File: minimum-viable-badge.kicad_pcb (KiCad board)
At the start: 2 copper layers, 100 x 64 mm, 34 parts, among them P1 BATTERY, P11 MECH, P12 MECH, P13 MECH, P2 USB, P301 eInk, Q1 S8050, Q2 S8050, SW3 ON|OFF, U1 CP2102, U2 ESP32-WROOM, U3 NCP5501, U4 MCP73831

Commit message: PCB new outline added
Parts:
- SW3: value ON|OFF -> OFF|ON
- moved P13 157.1 mm to (26.2, 93.9)
- moved P11 156.8 mm to (26.5, 41.8)
- moved P301 153.1 mm to (45.0, 60.5)
- moved U2 139.7 mm to (124.6, 84.5), turned to 45 degrees
- moved P12 137.2 mm to (133.5, 42.5)
- moved P2 73.9 mm to (124.2, 38.5), turned to 270 degrees
- moved SW3 73.3 mm to (110.6, 40.1), turned to 0 degrees
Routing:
- net (no net): track 203.8 -> 0.00 mm
- net /USB_VCC: track 182.7 -> 0.00 mm, vias 4 -> 0
- net +3V3: track 166.8 -> 0.00 mm, vias 2 -> 0
- net /BAT+: track 91.3 -> 0.00 mm, vias 2 -> 0
- net /USB_D+: track 90.1 -> 0.00 mm, vias 1 -> 0
- net /USB_D-: track 90.0 -> 0.00 mm, vias 1 -> 0
- net GND: track 75.8 -> 0.00 mm, vias 12 -> 0
- net /IO32: track 74.1 -> 0.00 mm
- net /IO33: track 72.5 -> 0.00 mm
- net /IO15: track 70.8 -> 0.00 mm, vias 1 -> 0
- net /D/C: track 70.7 -> 0.00 mm
- net /DTR: track 69.6 -> 0.00 mm, vias 2 -> 0
- net /IO12: track 69.6 -> 0.00 mm, vias 1 -> 0
- net /IO26: track 68.9 -> 0.00 mm
- net /CS: track 67.4 -> 0.00 mm
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- removed copper zone on B.Cu, net GND
- removed copper zone on F.Cu, net GND
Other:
- board size 100 x 64 mm -> 256.9 x 71.3 mm

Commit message: Placement started
Predicting Bob will end up changing all this
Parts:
- removed C1, C3: 10uF, Capacitors_SMD:C_0805_HandSoldering
- removed C13, C16: 4u7, Capacitors_SMD:C_0805_HandSoldering
- removed C14, C2, C4: 0.1uF, Capacitors_SMD:C_0603_HandSoldering
- removed C15: 100uF, Capacitors_SMD:C_1210_HandSoldering
- removed D1, D2: SS14, Diodes_SMD:D_SMA
- removed D3: CHRG, LEDs:LED_0603
- removed F1: 1A PTC, Diodes_SMD:D_1206
- removed P1: BATTERY, Pin_Headers:Pin_Header_Angled_1x02_Pitch2.54mm
- removed P11, P12, P13: MECH, Mounting_Holes:MountingHole_3.2mm_M3_Pad
- removed P2: USB, libs:USB-MICRO-5pin_PTHMOUNT-Amphenol.10118194-0001LF
- removed Q1, Q2: S8050, TO_SOT_Packages_SMD:SOT-23_Handsoldering
- removed R1: 1M, Resistors_SMD:R_0603_HandSoldering
- removed R10, R6: 470R, Resistors_SMD:R_0603_HandSoldering
- removed R12: 2K, Resistors_SMD:R_0603_HandSoldering
- removed R2: 100K, Resistors_SMD:R_0603_HandSoldering
- removed R3, R4: 12K(1%), Resistors_SMD:R_0603_HandSoldering
- removed R5: 10K, Resistors_SMD:R_0603_HandSoldering
- removed R7: 12K, Resistors_SMD:R_0603_HandSoldering
- removed SW3: OFF|ON, libs:SS12D00
- removed U1: CP2102, Housings_DFN_QFN:QFN-28-1EP_5x5mm_Pitch0.5mm
- removed U2: ESP32-WROOM, ESP32-footprints-Lib:ESP32-WROOM
- removed U3: NCP5501, libs:DPAK3.NCP5501
- removed U4: MCP73831, TO_SOT_Packages_SMD:SOT-23-5_HandSoldering
- added C101: 1uF, Capacitors_SMD:C_0603_HandSoldering, F.Cu at (129.9, 134.2)
- added C102: 1uF, Capacitors_SMD:C_0603_HandSoldering, F.Cu at (137.3, 133.5)
- added C103: 1uF, Capacitors_SMD:C_0603_HandSoldering, F.Cu at (135.8, 75.3)
- added C104: 10uF, Capacitors_SMD:C_0805_HandSoldering, F.Cu at (129.6, 60.8)
- added C105: 0.1uF, Capacitors_SMD:C_0603_HandSoldering, F.Cu at (129.7, 56.2)
- added C106: 10uF, Capacitors_SMD:C_0805_HandSoldering, F.Cu at (135.7, 65.2)
- added C107: 0.1uF, Capacitors_SMD:C_0603_HandSoldering, F.Cu at (135.9, 60.2)
- added C201: 4u7, Capacitors_SMD:C_0805_HandSoldering, F.Cu at (112.8, 43.6)
- added C202: 4u7, Capacitors_SMD:C_0805_HandSoldering, F.Cu at (99.7, 45.2)
- added C203: 0.1uF, Capacitors_SMD:C_0603_HandSoldering, F.Cu at (56.2, 45.8)
- added C204: 100uF, Capacitors_SMD:C_1210_HandSoldering, F.Cu at (55.9, 40.0)
- added C301: 1uF, Capacitors_SMD:C_0603_HandSoldering, F.Cu at (73.8, 182.4)
- added C302: 1uF 50V, Capacitors_SMD:C_0603_HandSoldering, F.Cu at (77.2, 167.8)
- added C303: 1uF 50V, Capacitors_SMD:C_0603_HandSoldering, F.Cu at (64.1, 182.1)
- added C304: 1uF, Capacitors_SMD:C_0603_HandSoldering, F.Cu at (67.2, 186.9)
- added C305: 1uF, Capacitors_SMD:C_0603_HandSoldering, F.Cu at (80.7, 172.6)
- added C306: 4.7uF 50V, Capacitors_SMD:C_0603_HandSoldering, F.Cu at (49.1, 186.3)
- added C307: 10uF 6.3V, Capacitors_SMD:C_0805_HandSoldering, F.Cu at (57.4, 175.3)
- added C308: 1uF, Capacitors_SMD:C_0603_HandSoldering, F.Cu at (75.3, 177.6)
- added C309: 1uF, Capacitors_SMD:C_0603_HandSoldering, F.Cu at (69.5, 182.1)
- added C310: 1uF, Capacitors_SMD:C_0603_HandSoldering, F.Cu at (62.9, 186.9)
- added C311: 1uF, Capacitors_SMD:C_0603_HandSoldering, F.Cu at (82.6, 167.8)
- added C312: 1uF, Capacitors_SMD:C_0603_HandSoldering, F.Cu at (85.0, 172.6)
- added D101: SS14, Diodes_SMD:D_SMA, F.Cu at (69.9, 143.7)
- added D201: SS14, Diodes_SMD:D_SMA, F.Cu at (80.6, 46.0)
- added D202: SS14, Diodes_SMD:D_SMA, F.Cu at (105.0, 39.3)
- added D203: CHRG, LEDs:LED_0603, F.Cu at (112.4, 38.7)
- added D301: SS14, Diodes_SMD:D_SMA, F.Cu at (70.1, 169.0)
- added D302: SS14, Diodes_SMD:D_SMA, F.Cu at (57.1, 181.6)
- added D303: SS14, Diodes_SMD:D_SMA, F.Cu at (65.1, 176.2)
- added F101: 1A PTC, Diodes_SMD:D_1206, F.Cu at (77.9, 143.3)
- added J101: EDGE_CONNECTOR, Pin_Headers:Pin_Header_Angled_1x10_Pitch2.54mm, F.Cu at (82.3, 91.1)
- added P101: USB, libs:USB-MICRO-5pin_PTHMOUNT-Amphenol.10118194-0001LF, F.Cu at (93.0, 38.6)
- added P102: BATTERY, Pin_Headers:Pin_Header_Angled_1x02_Pitch2.54mm, F.Cu at (72.4, 152.3)
- added P103: POT_LONG, libs:sense_long, B.Cu at (209.6, 57.6)
- added P104: BUTTON_A, Mounting_Holes:MountingHole_3.2mm_M3_Pad, B.Cu at (224.5, 77.1)
- added P105: BUTTON_B, Mounting_Holes:MountingHole_3.2mm_M3_Pad, B.Cu at (232.2, 77.1)
- added P106: POT_SHORT, libs:sense_short, B.Cu at (257.9, 61.5)
- added P107: MECH, Mounting_Holes:MountingHole_3.2mm_M3_Pad, F.Cu at (26.1, 42.1)
- added P108: MECH, Mounting_Holes:MountingHole_3.2mm_M3_Pad, F.Cu at (25.8, 94.2)
- added P109: MECH, Mounting_Holes:MountingHole_3.2mm_M3_Pad, F.Cu at (133.8, 42.0)
- added Q101: S8050, TO_SOT_Packages_SMD:SOT-23_Handsoldering, F.Cu at (124.0, 59.1)
- added Q102: S8050, TO_SOT_Packages_SMD:SOT-23_Handsoldering, F.Cu at (117.0, 59.1)
- added Q201: FDN340P, libs:SOT23_FET, F.Cu at (88.0, 46.7)
- added Q301: IRLML0030TRPBF, TO_SOT_Packages_SMD:SOT-23, F.Cu at (59.9, 169.0)
- added R101: 470R, Resistors_SMD:R_0603_HandSoldering, F.Cu at (129.4, 129.2)
- added R102: 470R, Resistors_SMD:R_0603_HandSoldering, F.Cu at (137.2, 128.7)
- added R103: 1M, Resistors_SMD:R_0603_HandSoldering, F.Cu at (110.1, 129.9)
- added R104: 100K, Resistors_SMD:R_0603_HandSoldering, F.Cu at (109.3, 148.3)
- added R105: 470R, Resistors_SMD:R_0603_HandSoldering, F.Cu at (128.9, 48.1)
- added R106: 12K, Resistors_SMD:R_0603_HandSoldering, F.Cu at (135.6, 70.7)
- added R107: 12K(1%), Resistors_SMD:R_0603_HandSoldering, F.Cu at (121.5, 53.0)
- added R108: 12K(1%), Resistors_SMD:R_0603_HandSoldering, F.Cu at (123.8, 65.1)
- added R201: 10K, Resistors_SMD:R_0603_HandSoldering, F.Cu at (92.5, 45.7)
- added R202: 2K, Resistors_SMD:R_0603_HandSoldering, F.Cu at (112.7, 48.1)
- added R203: 470R, Resistors_SMD:R_0603_HandSoldering, F.Cu at (117.1, 38.7)
- added R301: 0R, Resistors_SMD:R_0603_HandSoldering, F.Cu at (71.0, 175.1)
- added R302: 0.47R, Resistors_SMD:R_0603_HandSoldering, F.Cu at (76.2, 172.8)
- added SW201: ON|OFF, libs:SS12D00, F.Cu at (81.1, 39.8)
- added U101: ESP32-WROOM, ESP32-footprints-Lib:ESP32-WROOM, F.Cu at (124.5, 84.6)
- added U102: CP2102, Housings_DFN_QFN:QFN-28-1EP_5x5mm_Pitch0.5mm, F.Cu at (135.9, 53.5)
- added U201: MCP73831, TO_SOT_Packages_SMD:SOT-23-5_HandSoldering, F.Cu at (105.2, 46.6)
- added U202: NCP5501, libs:DPAK3.NCP5501, F.Cu at (67.0, 42.5)
- moved P301 4.72 mm to (44.5, 55.8)
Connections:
- net Net-(P4-Pad18) renamed /E-Ink Display/TSDA
- net Net-(P4-Pad19) renamed /E-Ink Display/TSCL
- net Net-(P4-Pad6) renamed /E-Ink Display/VPP
- P301 pad 1: Net-(P4-Pad1) -> /E-Ink Display/VCOM
- P301 pad 10: /CS -> +3V3
- P301 pad 11: /IO26 -> /EINK_MOSI
- P301 pad 12: /D/C -> /EINK_SCLK
- P301 pad 13: /IO33 -> /EINK_CS
- P301 pad 14: /IO32 -> /EINK_D/C
- P301 pad 15: +3V3 -> /EINK_RST
- P301 pad 16: +3V3 -> /EINK_BUSY
- P301 pad 2: Net-(P4-Pad2) -> /E-Ink Display/PREVGL
- P301 pad 20: Net-(P4-Pad20) -> /E-Ink Display/VGH
- P301 pad 21: Net-(P4-Pad21) -> /E-Ink Display/VGL
- P301 pad 22: Net-(P4-Pad22) -> /E-Ink Display/RESE
- P301 pad 23: Net-(P4-Pad23) -> /E-Ink Display/GDR
- P301 pad 3: Net-(P4-Pad3) -> /E-Ink Display/VSL
- P301 pad 4: Net-(P4-Pad4) -> /E-Ink Display/PREVGH
- P301 pad 5: Net-(P4-Pad5) -> /E-Ink Display/VSH
- P301 pad 7: Net-(P4-Pad7) -> /E-Ink Display/LCD_VDD
- P301 pad 8: Net-(P4-Pad8) -> GND
- P301 pad 9: Net-(P4-Pad9) -> +3V3
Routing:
- net /EN: track 0.00 -> 32.8 mm
- net /RTS: track 0.00 -> 28.3 mm, vias 0 -> 2
- net /DTR: track 0.00 -> 21.9 mm
- net +3V3: track 0.00 -> 20.3 mm
- net /USB_VCC: track 0.00 -> 9.73 mm
- net Net-(Q102-Pad1): track 0.00 -> 7.27 mm
- net Net-(R105-Pad2): track 0.00 -> 6.98 mm
- net Net-(Q101-Pad1): track 0.00 -> 5.28 mm
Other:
- board size 256.9 x 71.3 mm -> 120 x 64 mm
- board text removed: "GND"
- board text removed: "https://github.com/mage0r/Minimum-viable-badge"

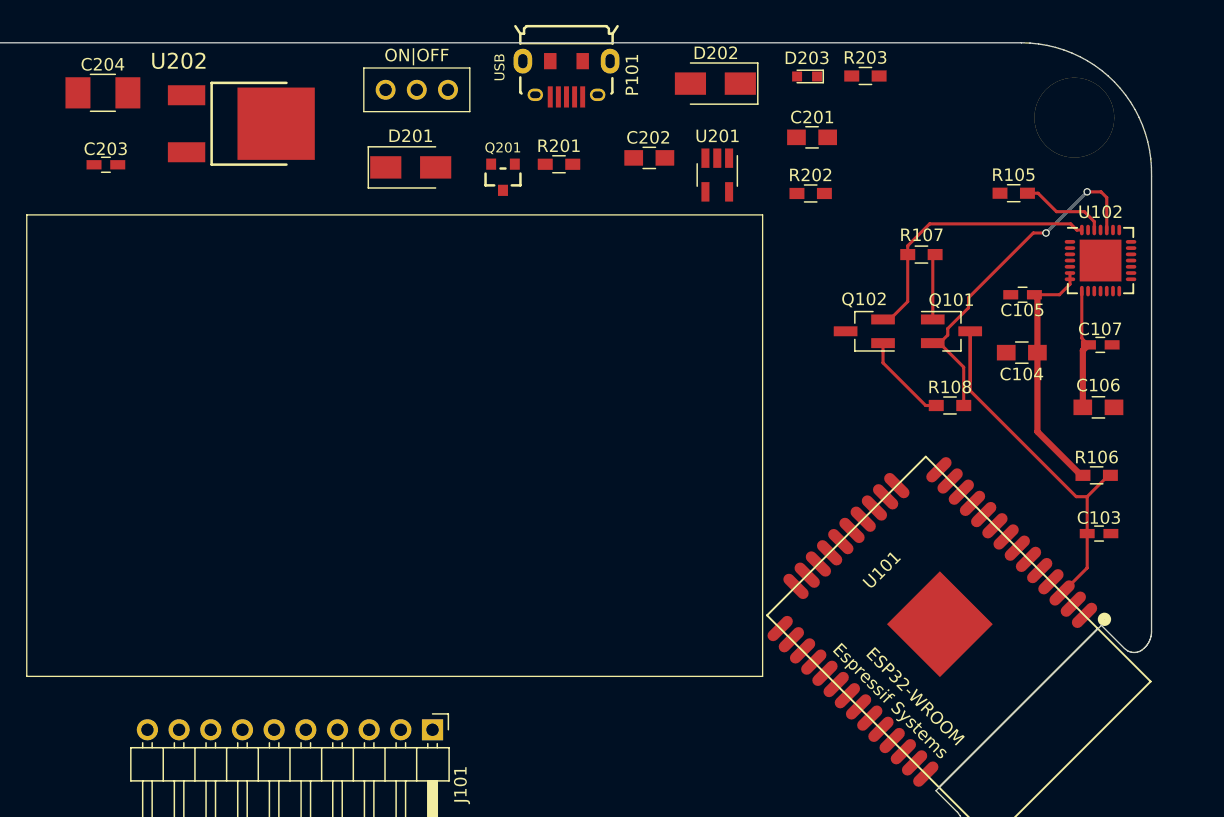
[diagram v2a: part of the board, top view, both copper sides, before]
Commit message: More footprint layout.
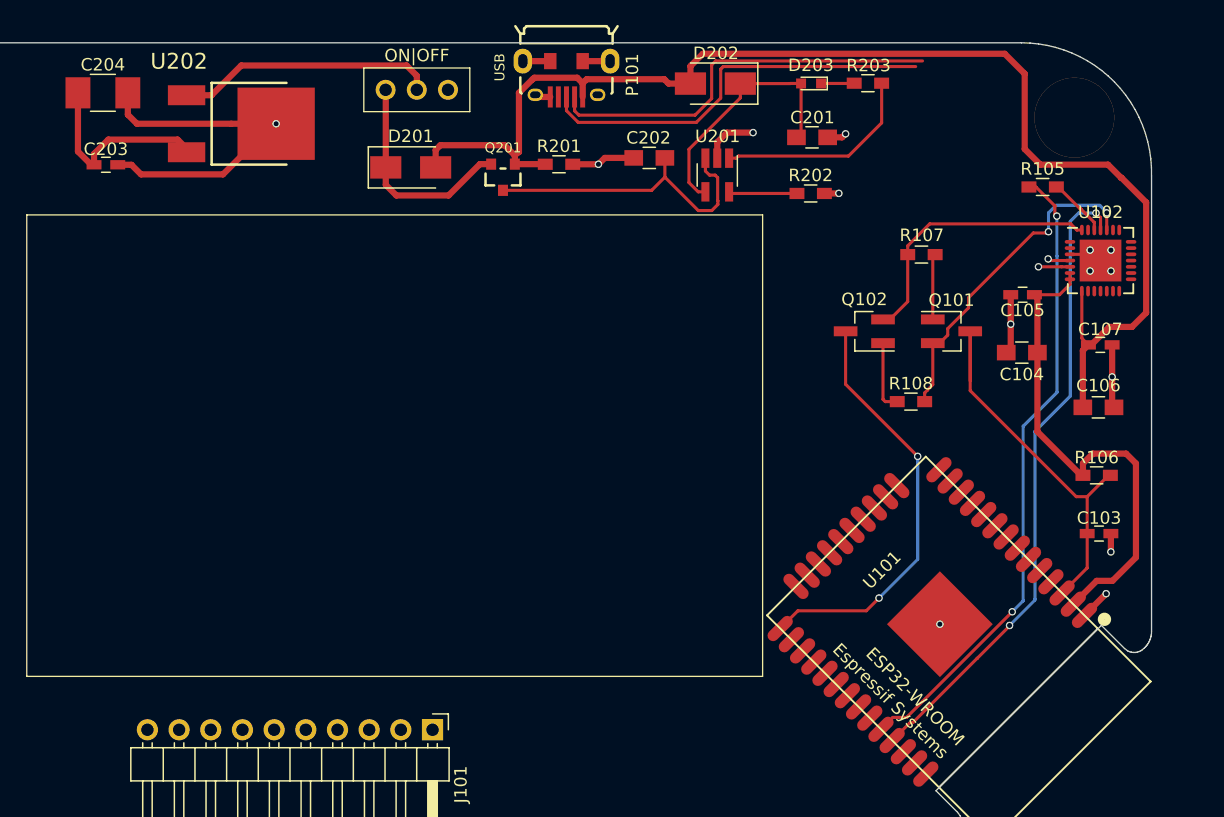
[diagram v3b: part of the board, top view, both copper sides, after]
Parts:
- moved R108 3.15 mm to (120.7, 64.8)
- moved R105 2.37 mm to (131.3, 47.6)
- moved D203 0.64 mm to (112.7, 39.3)
- moved R203 0.61 mm to (117.3, 39.2), turned to 180 degrees
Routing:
- net /USB_VCC: track 9.73 -> 108.2 mm
- net GND: track 0.00 -> 62.1 mm, vias 0 -> 14
- net /RXD: track 0.00 -> 51.5 mm, vias 0 -> 2
- net /TXD: track 0.00 -> 51.2 mm, vias 0 -> 2
- net +3V3: track 20.3 -> 56.0 mm
- net /USB_D-: track 0.00 -> 35.1 mm, vias 0 -> 1
- net /USB_D+: track 0.00 -> 34.5 mm, vias 0 -> 1
- net /IO0: track 0.00 -> 34.0 mm, vias 0 -> 2
- net /BAT+: track 0.00 -> 24.9 mm
- net Net-(SW201-Pad2): track 0.00 -> 20.9 mm
- net Net-(C201-Pad1): track 0.00 -> 20.7 mm
- net /hipster-power/UNREG_V: track 0.00 -> 17.5 mm
- net Net-(R203-Pad1): track 0.00 -> 16.6 mm
- net Net-(R202-Pad1): track 0.00 -> 5.49 mm
- net Net-(D203-Pad1): track 0.00 -> 2.67 mm
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
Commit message: Keeping everything in sync.
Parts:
- added L301: 68uH 410MA, Capacitors_SMD:C_1210_HandSoldering, F.Cu at (48.0, 39.2)
- added SW101: PRGM, libs:K2-1107st, F.Cu at (126.2, 122.8)
- added SW102: RESET, libs:K2-1107st, F.Cu at (146.1, 122.7)
- R201: value 10K -> 12K
- R302: value 0.47R -> 0.47R, 1%
- moved Q301 123.6 mm to (50.8, 45.8), turned to 90 degrees
- moved R102 11.7 mm to (148.9, 128.4)
- moved C101 8.27 mm to (123.4, 129.1), turned to 180 degrees
- moved C102 7.85 mm to (143.3, 128.4), turned to 180 degrees
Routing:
- net /USB_D+: track 34.5 -> 58.3 mm, vias 1 -> 4
- net /USB_D-: track 35.1 -> 57.9 mm, vias 1 -> 2

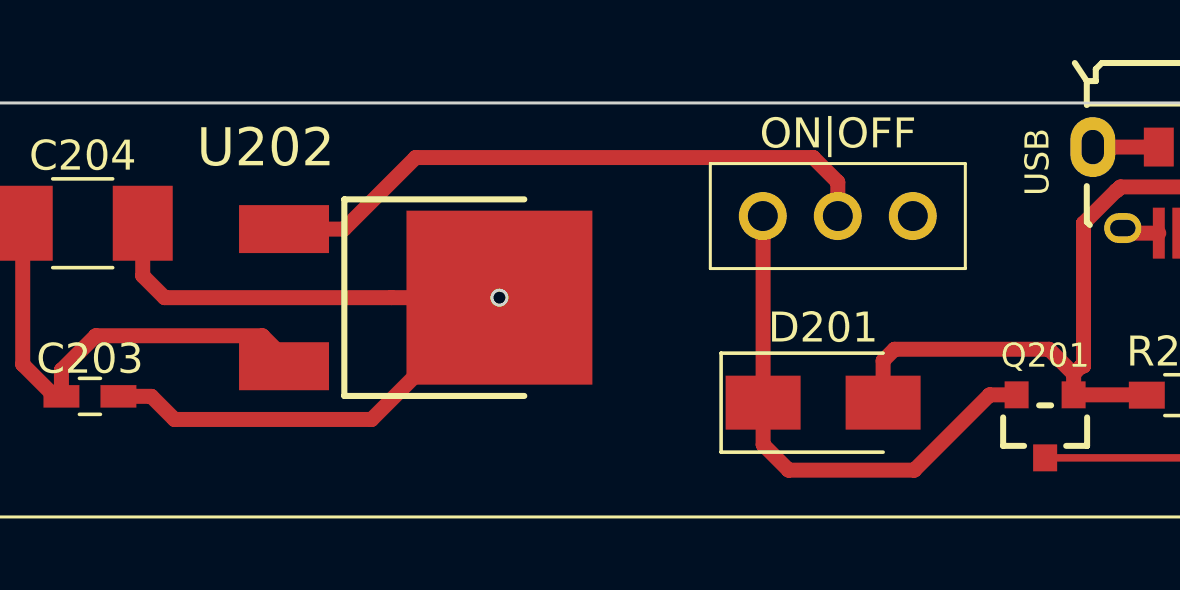
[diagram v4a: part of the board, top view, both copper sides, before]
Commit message: Updated to use new switch.
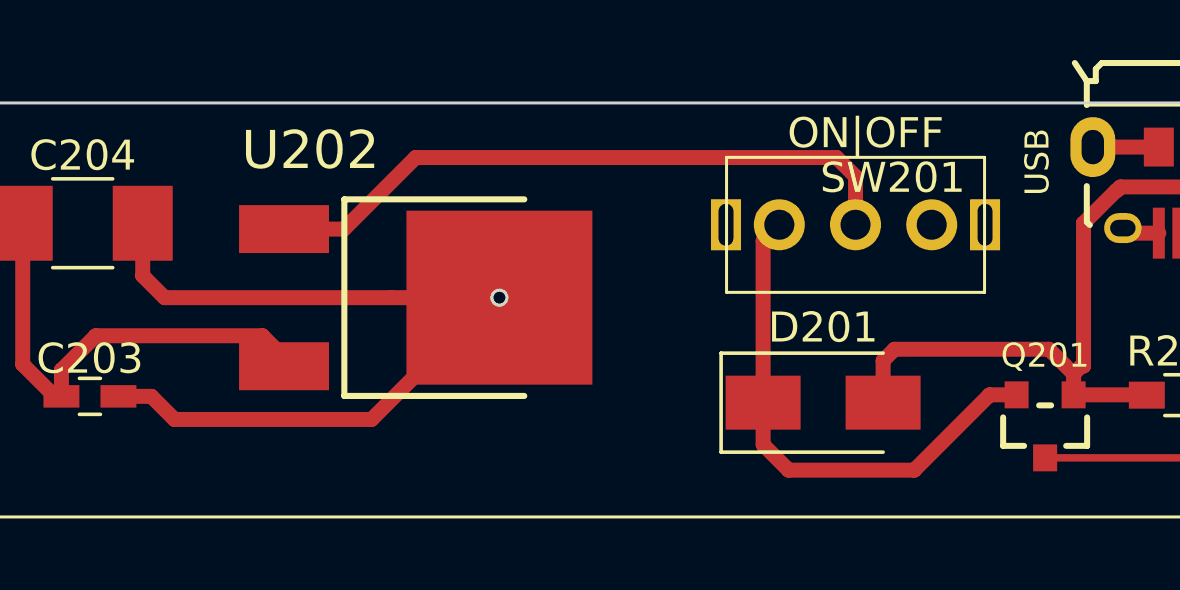
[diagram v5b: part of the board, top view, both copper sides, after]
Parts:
- SW201: footprint libs:SS12D00 -> libs:SK12D07VG5
- moved SW201 0.66 mm to (81.7, 40.1)
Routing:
- net Net-(SW201-Pad2): track 20.9 -> 21.9 mm
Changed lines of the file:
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@@
   (general
     (links 175)
-    (no_connects 127)
+    (no_connects 126)
     (area 19.94251 35.949999 140.050001 100.050001)
     (thickness 1.6)
     (drawings 156)
-    (tracks 291)
+    (tracks 292)
     (zones 0)
     (modules 67)
@@
   )
   (setup
-    (last_trace_width 0.25)
+    (last_trace_width 0.5)
     (user_trace_width 0.25)
     (user_trace_width 0.5)
@@
     )
   )
-  (module libs:SS12D00 (layer F.Cu)
-    (at 81.09 39.77)
-    (fp_text reference SW201 (at 0 2.5) (layer F.SilkS) hide
-      (effects (font (size 0.8 0.8) (thickness 0.12)))
-    )
-    (fp_text value ON|OFF (at 0.00762 -2.75082) (layer F.SilkS)
-      (effects (font (size 1 1) (thickness 0.15)))
-    )
-    (fp_line (start -4.25 1.75) (end -4.25 -1.75) (layer F.SilkS) (width 0.1))
-    (fp_line (start 4.25 1.75) (end -4.25 1.75) (layer F.SilkS) (width 0.1))
-    (fp_line (start 4.25 -1.75) (end 4.25 1.75) (layer F.SilkS) (width 0.1))
-    (fp_line (start -4.25 -1.75) (end 4.25 -1.75) (layer F.SilkS) (width 0.1))
-    (pad 2 thru_hole circle (at 0 0) (size 1.6 1.6) (drill 1) (layers *.Cu *.Mask F.SilkS)
-      (net 74 "Net-(SW201-Pad2)"))
-    (pad 1 thru_hole circle (at -2.5 0) (size 1.6 1.6) (drill 1) (layers *.Cu *.Mask F.SilkS)
-      (net 45 /hipster-power/UNREG_V))
-    (pad 3 thru_hole circle (at 2.5 0) (size 1.6 1.6) (drill 1) (layers *.Cu *.Mask F.SilkS))
-  )
   (module Housings_DFN_QFN:QFN-28-1EP_5x5mm_Pitch0.5mm (layer F.Cu)
     (at 135.91 53.46)
@@
     (at 67.02 42.49 270)
     (descr <b>DPAK</b><p>)
-    (fp_text reference U202 (at -5 5 540) (layer F.SilkS)
+    (fp_text reference U202 (at -4.91 3.51 540) (layer F.SilkS)
       (effects (font (size 1.27 1.27) (thickness 0.1016)))
     )
@@
       (net 32 "Net-(C102-Pad1)"))
   )
+  (module libs:SK12D07VG5 (layer F.Cu)
+    (at 81.68 40.06)
+    (fp_text reference SW201 (at 1.24 -1.56) (layer F.SilkS)
+      (effects (font (size 1 1) (thickness 0.15)))
+    )
+    (fp_text value ON|OFF (at 0.34 -3.05) (layer F.SilkS)
+      (effects (font (size 1 1) (thickness 0.15)))
+    )
+    (fp_line (start -4.2989 -2.2464) (end 4.3011 -2.2464) (layer F.SilkS) (width 0.1))
+    (fp_line (start 4.3011 -0.5964) (end 4.3011 0.6036) (layer F.SilkS) (width 0.1))
+    (fp_line (start 4.3011 -2.2464) (end 4.3011 -0.5964) (layer F.SilkS) (width 0.1))
+    (fp_line (start -4.2989 2.2536) (end -4.2989 0.6036) (layer F.SilkS) (width 0.1))
+    (fp_line (start 4.3011 0.6036) (end 4.3011 2.2536) (layer F.SilkS) (width 0.1))
+    (fp_line (start 4.3011 2.2536) (end -4.2989 2.2536) (layer F.SilkS) (width 0.1))
+    (fp_line (start -4.2989 -0.5964) (end -4.2989 -2.2464) (layer F.SilkS) (width 0.1))
+    (fp_line (start -4.2989 0.6036) (end -4.2989 -0.5964) (layer F.SilkS) (width 0.1))
+    (fp_line (start 0.0011 -3.7464) (end 2.0511 -3.7464) (layer Eco2.User) (width 0.1))
+    (fp_line (start -2.0489 -3.7464) (end 0.0011 -3.7464) (layer Eco2.User) (width 0.1))
+    (fp_line (start 0.0011 -2.2464) (end 0.0011 -3.7464) (layer Eco2.User) (width 0.1))
+    (fp_line (start 2.0511 -3.7464) (end 2.0511 -2.2464) (layer Eco2.User) (width 0.1))
+    (fp_line (start 0.0011 -3.7464) (end 0.0011 -2.2464) (layer Eco2.User) (width 0.1))
+    (fp_line (start -2.0489 -2.2464) (end -2.0489 -3.7464) (layer Eco2.User) (width 0.1))
+    (pad 2 thru_hole circle (at 0 0) (size 1.7 1.7) (drill 1) (layers *.Cu *.Mask)
+      (net 74 "Net-(SW201-Pad2)"))
+    (pad 3 thru_hole circle (at 2.54 0) (size 1.7 1.7) (drill 1) (layers *.Cu *.Mask))
+    (pad 1 thru_hole circle (at -2.54 0) (size 1.7 1.7) (drill 1) (layers *.Cu *.Mask)
+      (net 45 /hipster-power/UNREG_V))
+    (pad "" thru_hole rect (at -4.318 0) (size 1 1.7) (drill oval 0.5 1.4) (layers *.Cu *.Mask))
+    (pad "" thru_hole rect (at 4.318 0) (size 1 1.7) (drill oval 0.5 1.4) (layers *.Cu *.Mask))
+  )
   (gr_line (start 38.530162 49.448447) (end 38.530162 40.112733) (layer B.SilkS) (width 0.1))
   (gr_line (start 38.530162 62.366304) (end 38.530162 49.448447) (layer B.SilkS) (width 0.1))
@@
   (segment (start 111.58 43.53) (end 111.53 43.58) (width 0.25) (layer F.Cu) (net 33))
   (segment (start 107.03 39.27) (end 111.01 39.27) (width 0.25) (layer F.Cu) (net 33))
-  (segment (start 78.6 45.99) (end 78.6 39.78) (width 0.5) (layer F.Cu) (net 45))
+  (segment (start 78.6 45.99) (end 78.6 40.6) (width 0.5) (layer F.Cu) (net 45))
+  (segment (start 78.6 40.6) (end 79.14 40.06) (width 0.5) (layer F.Cu) (net 45))
   (segment (start 78.6 39.78) (end 78.59 39.77) (width 0.5) (layer F.Cu) (net 45))
   (segment (start 79.45 48.24) (end 83.63923 48.24) (width 0.5) (layer F.Cu) (net 45))
@@
   (segment (start 106.875 45.08) (end 106.705 45.25) (width 0.25) (layer F.Cu) (net 73))
   (segment (start 106.705 45.25) (end 106.13 45.25) (width 0.25) (layer F.Cu) (net 73))
-  (segment (start 80.27137 37.82) (end 67.015 37.82) (width 0.5) (layer F.Cu) (net 74))
-  (segment (start 67.015 37.82) (end 64.63 40.205) (width 0.5) (layer F.Cu) (net 74))
-  (segment (start 64.63 40.205) (end 62.63 40.205) (width 0.5) (layer F.Cu) (net 74))
-  (segment (start 81.09 39.77) (end 81.09 38.63863) (width 0.5) (layer F.Cu) (net 74))
-  (segment (start 81.09 38.63863) (end 80.27137 37.82) (width 0.5) (layer F.Cu) (net 74))
+  (segment (start 62.63 40.205) (end 64.63 40.205) (width 0.5) (layer F.Cu) (net 74))
+  (segment (start 64.63 40.205) (end 67.015 37.82) (width 0.5) (layer F.Cu) (net 74))
+  (segment (start 67.015 37.82) (end 81.05 37.82) (width 0.5) (layer F.Cu) (net 74))
+  (segment (start 81.05 37.82) (end 81.68 38.45) (width 0.5) (layer F.Cu) (net 74))
+  (segment (start 81.68 38.45) (end 81.68 40.06) (width 0.5) (layer F.Cu) (net 74))
 )
